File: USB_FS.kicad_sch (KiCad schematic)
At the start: 5 parts, among them U8 USB-TYPE-C-016

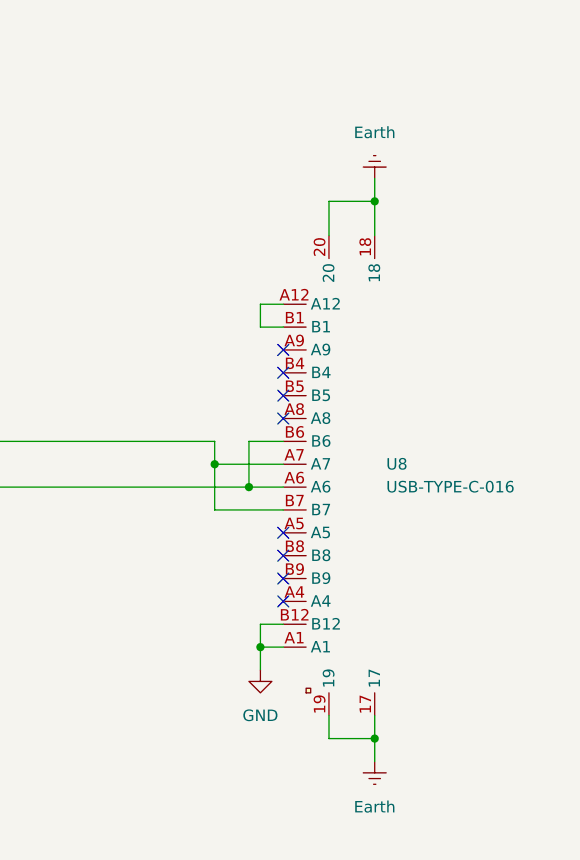
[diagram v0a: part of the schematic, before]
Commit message: Key CHanges for connector choices , termination and semi-final decisions on them
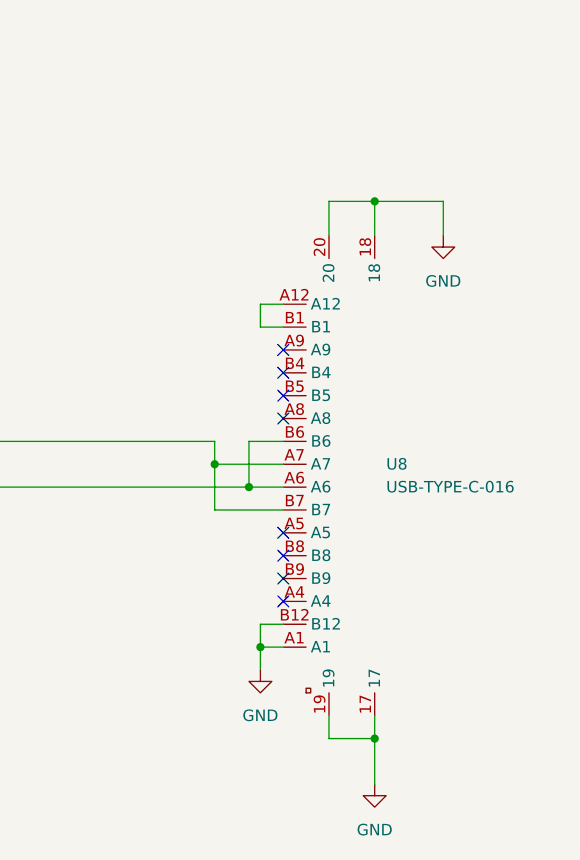
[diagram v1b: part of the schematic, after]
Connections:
- net Earth is gone; now on net GND: U8.17, U8.18, U8.19, U8.20
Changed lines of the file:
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@@
+	)
+	(junction
+		(at 163.83 72.39)
+		(diameter 0)
+		(color 0 0 0 0)
 	)
 	(junction
@@
 		(color 0 0 0 0)
 	)
-	(junction
-		(at 163.83 72.39)
-		(diameter 0)
-		(color 0 0 0 0)
-	)
 	(no_connect
 		(at 167.64 80.01)
@@
 	(wire
 		(pts
-			(xy 177.8 102.87) (xy 177.8 100.33)
+			(xy 177.8 100.33) (xy 177.8 105.41)
 		)
 		(stroke
@@
 	(wire
 		(pts
+			(xy 185.42 40.64) (xy 185.42 44.45)
+		)
+		(stroke
+			(width 0)
+			(type default)
+		)
+	)
+	(wire
+		(pts
 			(xy 160.02 69.85) (xy 167.64 69.85)
 		)
@@
 	(wire
 		(pts
+			(xy 185.42 40.64) (xy 177.8 40.64)
+		)
+		(stroke
+			(width 0)
+			(type default)
+		)
+	)
+	(wire
+		(pts
 			(xy 163.83 72.39) (xy 167.64 72.39)
 		)
@@
 		(pts
 			(xy 165.1 87.63) (xy 165.1 90.17)
-		)
-		(stroke
-			(width 0)
-			(type default)
-		)
-	)
-	(wire
-		(pts
-			(xy 177.8 40.64) (xy 177.8 38.1)
 		)
 		(stroke
@@
 			)
 			(justify right)
+		)
+	)
+	(symbol
+		(lib_id "power:GND")
+		(at 185.42 44.45 0)
+		(unit 1)
+		(exclude_from_sim no)
+		(in_bom yes)
+		(on_board yes)
+		(dnp no)
+		(fields_autoplaced yes)
+		(property "Reference" "#PWR060"
+			(at 185.42 50.8 0)
+			(effects
+				(font
+					(size 1.27 1.27)
+				)
+				(hide yes)
+			)
+		)
+		(property "Value" "GND"
+			(at 185.42 49.53 0)
+			(effects
+				(font
+					(size 1.27 1.27)
+				)
+			)
+		)
+		(property "Footprint" ""
+			(at 185.42 44.45 0)
+			(effects
+				(font
+					(size 1.27 1.27)
+				)
+				(hide yes)
+			)
+		)
+		(property "Datasheet" ""
+			(at 185.42 44.45 0)
+			(effects
+				(font
+					(size 1.27 1.27)
+				)
+				(hide yes)
+			)
+		)
+		(property "Description" "Power symbol creates a global label with name \"GND\" , ground"
+			(at 185.42 44.45 0)
+			(effects
+				(font
+					(size 1.27 1.27)
+				)
+				(hide yes)
+			)
+		)
+		(pin "1"
+		)
+		(instances
+			(project "OhWare"
+				(path "/38f33acd-ac87-4918-9c1f-d78977d10c9f/89bfa8b8-f922-4671-b743-8eba341d6056"
+					(reference "#PWR060")
+					(unit 1)
+				)
+			)
 		)
 	)
@@
 	)
 	(symbol
-		(lib_id "power:Earth")
-		(at 177.8 38.1 0)
-		(mirror x)
-		(unit 1)
-		(exclude_from_sim no)
-		(in_bom yes)
-		(on_board yes)
-		(dnp no)
-		(fields_autoplaced yes)
-		(property "Reference" "#PWR091"
-			(at 177.8 31.75 0)
-			(effects
-				(font
-					(size 1.27 1.27)
-				)
-				(hide yes)
-			)
-		)
-		(property "Value" "Earth"
-			(at 177.8 33.02 0)
-			(effects
-				(font
-					(size 1.27 1.27)
-				)
-			)
-		)
-		(property "Footprint" ""
-			(at 177.8 38.1 0)
-			(effects
-				(font
-					(size 1.27 1.27)
-				)
-				(hide yes)
-			)
-		)
-		(property "Datasheet" "~"
-			(at 177.8 38.1 0)
-			(effects
-				(font
-					(size 1.27 1.27)
-				)
-				(hide yes)
-			)
-		)
-		(property "Description" "Power symbol creates a global label with name \"Earth\""
-			(at 177.8 38.1 0)
-			(effects
-				(font
-					(size 1.27 1.27)
-				)
-				(hide yes)
-			)
-		)
-		(pin "1"
-		)
-		(instances
-			(project "OhWare"
-				(path "/38f33acd-ac87-4918-9c1f-d78977d10c9f/89bfa8b8-f922-4671-b743-8eba341d6056"
-					(reference "#PWR091")
-					(unit 1)
-				)
-			)
-		)
-	)
-	(symbol
-		(lib_id "power:Earth")
-		(at 177.8 102.87 0)
-		(unit 1)
-		(exclude_from_sim no)
-		(in_bom yes)
-		(on_board yes)
-		(dnp no)
-		(fields_autoplaced yes)
-		(property "Reference" "#PWR041"
-			(at 177.8 109.22 0)
-			(effects
-				(font
-					(size 1.27 1.27)
-				)
-				(hide yes)
-			)
-		)
-		(property "Value" "Earth"
-			(at 177.8 107.95 0)
-			(effects
-				(font
-					(size 1.27 1.27)
-				)
-			)
-		)
-		(property "Footprint" ""
-			(at 177.8 102.87 0)
-			(effects
-				(font
-					(size 1.27 1.27)
-				)
-				(hide yes)
-			)
-		)
-		(property "Datasheet" "~"
-			(at 177.8 102.87 0)
-			(effects
-				(font
-					(size 1.27 1.27)
-				)
-				(hide yes)
-			)
-		)
-		(property "Description" "Power symbol creates a global label with name \"Earth\""
-			(at 177.8 102.87 0)
-			(effects
-				(font
-					(size 1.27 1.27)
-				)
-				(hide yes)
-			)
-		)
-		(pin "1"
-		)
-		(instances
-			(project "OhWare"
-				(path "/38f33acd-ac87-4918-9c1f-d78977d10c9f/89bfa8b8-f922-4671-b743-8eba341d6056"
-					(reference "#PWR041")
-					(unit 1)
-				)
-			)
-		)
-	)
-	(symbol
 		(lib_id "Device:C")
 		(at 78.74 74.93 0)
@@
 					(unit 1)
 				)
+			)
+		)
+	)
+	(symbol
+		(lib_id "power:GND")
+		(at 177.8 105.41 0)
+		(unit 1)
+		(exclude_from_sim no)
+		(in_bom yes)
+		(on_board yes)
+		(dnp no)
+		(fields_autoplaced yes)
+		(property "Reference" "#PWR041"
+			(at 177.8 111.76 0)
+			(effects
+				(font
+					(size 1.27 1.27)
+				)
+				(hide yes)
+			)
+		)
+		(property "Value" "GND"
+			(at 177.8 110.49 0)
+			(effects
+				(font
+					(size 1.27 1.27)
+				)
+			)
+		)
+		(property "Footprint" ""
+			(at 177.8 105.41 0)
+			(effects
+				(font
+					(size 1.27 1.27)
+				)
+				(hide yes)
+			)
+		)
+		(property "Datasheet" ""
+			(at 177.8 105.41 0)
+			(effects
+				(font
+					(size 1.27 1.27)
+				)
+				(hide yes)
+			)
+		)
+		(property "Description" "Power symbol creates a global label with name \"GND\" , ground"
+			(at 177.8 105.41 0)
+			(effects
+				(font
+					(size 1.27 1.27)
+				)
+				(hide yes)
+			)
+		)
+		(pin "1"
+		)
+		(instances
+			(project "OhWare"
+				(path "/38f33acd-ac87-4918-9c1f-d78977d10c9f/89bfa8b8-f922-4671-b743-8eba341d6056"
+					(reference "#PWR041")
+					(unit 1)
+				)

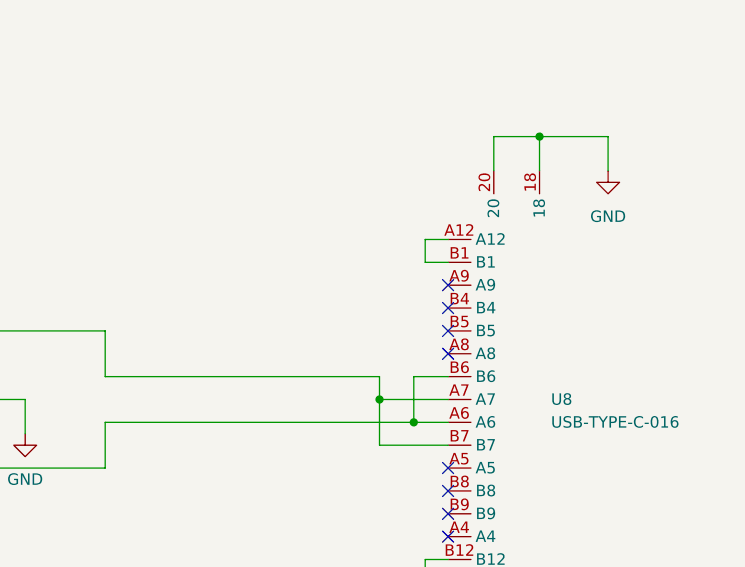
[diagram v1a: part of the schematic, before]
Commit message: Done routing for Buck Converter , Rs485 and CAN , Some Routing for MCU and associated circuitry , NO ETHERNET ROUTING , NO module Interconnects yet
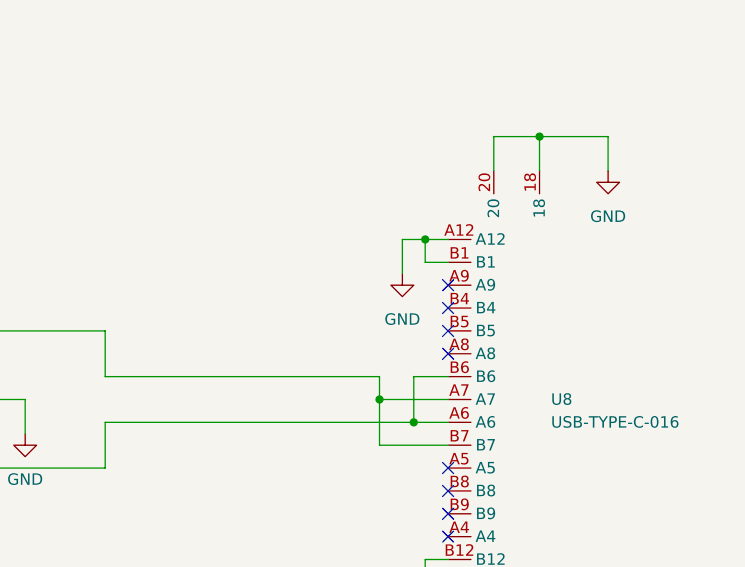
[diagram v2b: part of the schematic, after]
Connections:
- net GND: now also U8.A12, U8.B1
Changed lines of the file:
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@@
+	)
+	(junction
+		(at 165.1 52.07)
+		(diameter 0)
+		(color 0 0 0 0)
 	)
 	(junction
@@
 	(wire
 		(pts
+			(xy 162.56 52.07) (xy 165.1 52.07)
+		)
+		(stroke
+			(width 0)
+			(type default)
+		)
+	)
+	(wire
+		(pts
 			(xy 163.83 67.31) (xy 163.83 72.39)
 		)
@@
 		(pts
 			(xy 165.1 90.17) (xy 165.1 92.71)
+		)
+		(stroke
+			(width 0)
+			(type default)
+		)
+	)
+	(wire
+		(pts
+			(xy 162.56 55.88) (xy 162.56 52.07)
 		)
 		(stroke
@@
 					(unit 1)
 				)
+			)
+		)
+	)
+	(symbol
+		(lib_id "power:GND")
+		(at 162.56 55.88 0)
+		(unit 1)
+		(exclude_from_sim no)
+		(in_bom yes)
+		(on_board yes)
+		(dnp no)
+		(fields_autoplaced yes)
+		(property "Reference" "#PWR069"
+			(at 162.56 62.23 0)
+			(effects
+				(font
+					(size 1.27 1.27)
+				)
+				(hide yes)
+			)
+		)
+		(property "Value" "GND"
+			(at 162.56 60.96 0)
+			(effects
+				(font
+					(size 1.27 1.27)
+				)
+			)
+		)
+		(property "Footprint" ""
+			(at 162.56 55.88 0)
+			(effects
+				(font
+					(size 1.27 1.27)
+				)
+				(hide yes)
+			)
+		)
+		(property "Datasheet" ""
+			(at 162.56 55.88 0)
+			(effects
+				(font
+					(size 1.27 1.27)
+				)
+				(hide yes)
+			)
+		)
+		(property "Description" "Power symbol creates a global label with name \"GND\" , ground"
+			(at 162.56 55.88 0)
+			(effects
+				(font
+					(size 1.27 1.27)
+				)
+				(hide yes)
+			)
+		)
+		(pin "1"
+		)
+		(instances
+			(project "OhWare"
+				(path "/38f33acd-ac87-4918-9c1f-d78977d10c9f/89bfa8b8-f922-4671-b743-8eba341d6056"
+					(reference "#PWR069")
+					(unit 1)
+				)

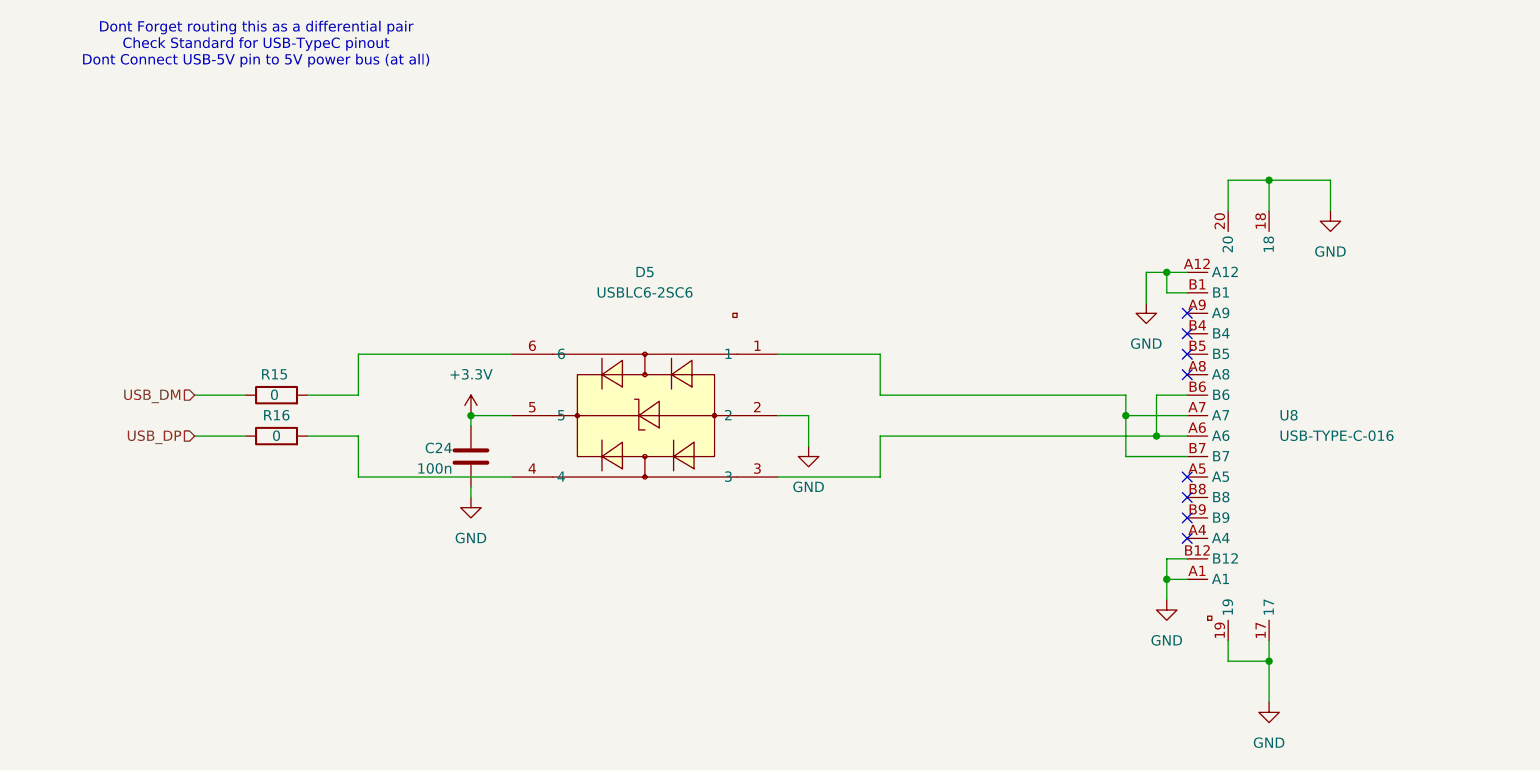
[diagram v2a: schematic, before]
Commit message: mcu circuit Done , + Ehernet Done (still placement is negotiable (best placement for minimal routing hustle))
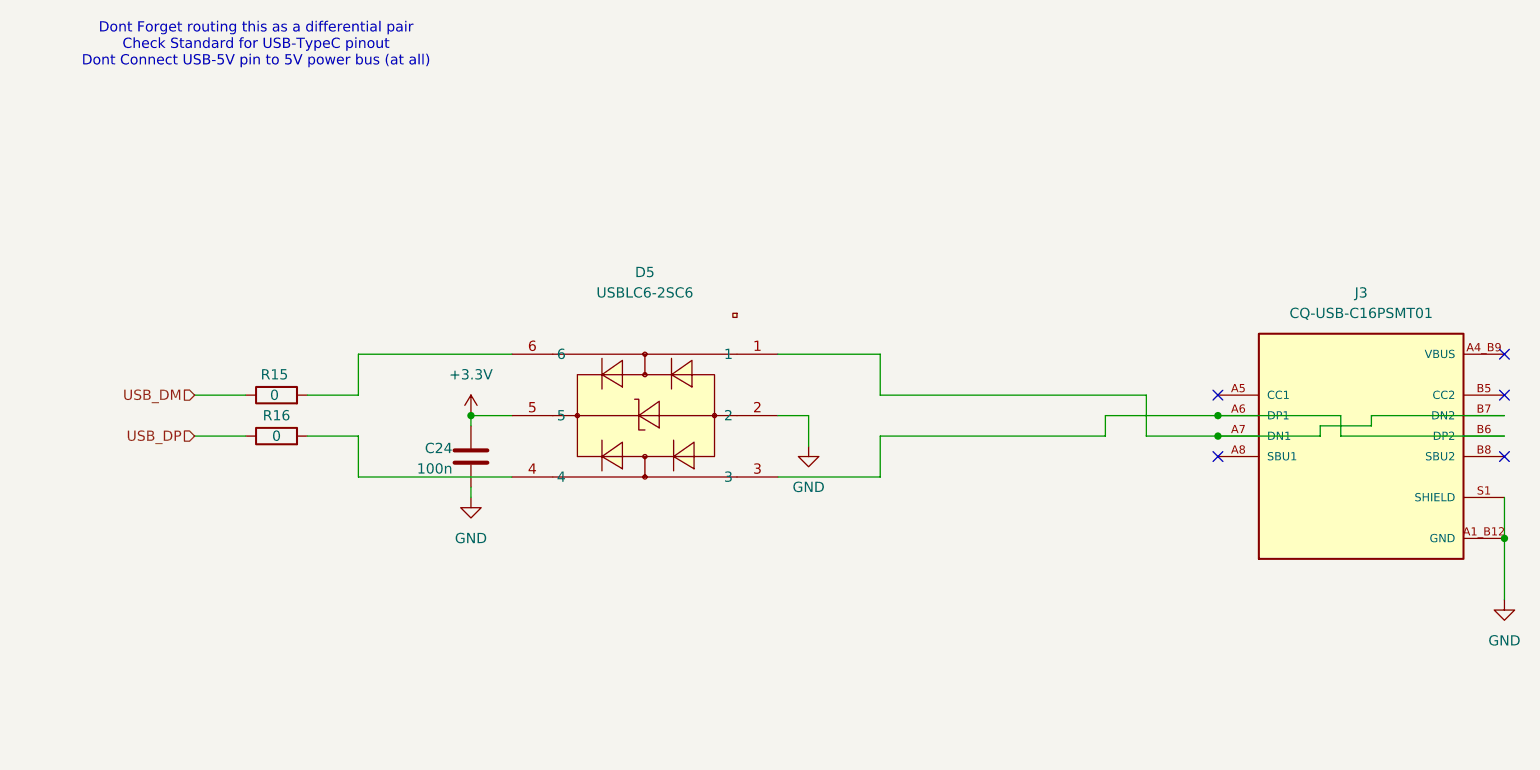
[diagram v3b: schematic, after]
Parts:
- removed U8: USB-TYPE-C-016, EasyEDA:USB-SMD_TYPE-C16PCB1.6073, symbol EasyEDA:USB-TYPE-C-016
- added J3: CQ-USB-C16PSMT01, EasyEDA:SHENZHEN-CHUANGQIN-TECHNOLOGY_CQ-USB-C16PSMT01, symbol EasyEDA:CQ-USB-C16PSMT01
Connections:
- net GND: now also J3.A1_B12 (GND), J3.B1_A12 (GND), J3.S1 (SHIELD), J3.S2 (SHIELD), J3.S3 (SHIELD), J3.S4 (SHIELD)
- net at D5.3: now also J3.A6 (DP1), J3.B6 (DP2)
- net at D5.1: now also J3.A7 (DN1), J3.B7 (DN2)
- new net VBUS: J3.A4_B9 (VBUS), J3.B4_A9 (VBUS)
- no-connect marks 8 -> 5
